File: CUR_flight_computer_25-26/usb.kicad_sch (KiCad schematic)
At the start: 4 parts, among them J1 USB_C_Receptacle_USB2.0_16P, U3 USBLC6-2SC6

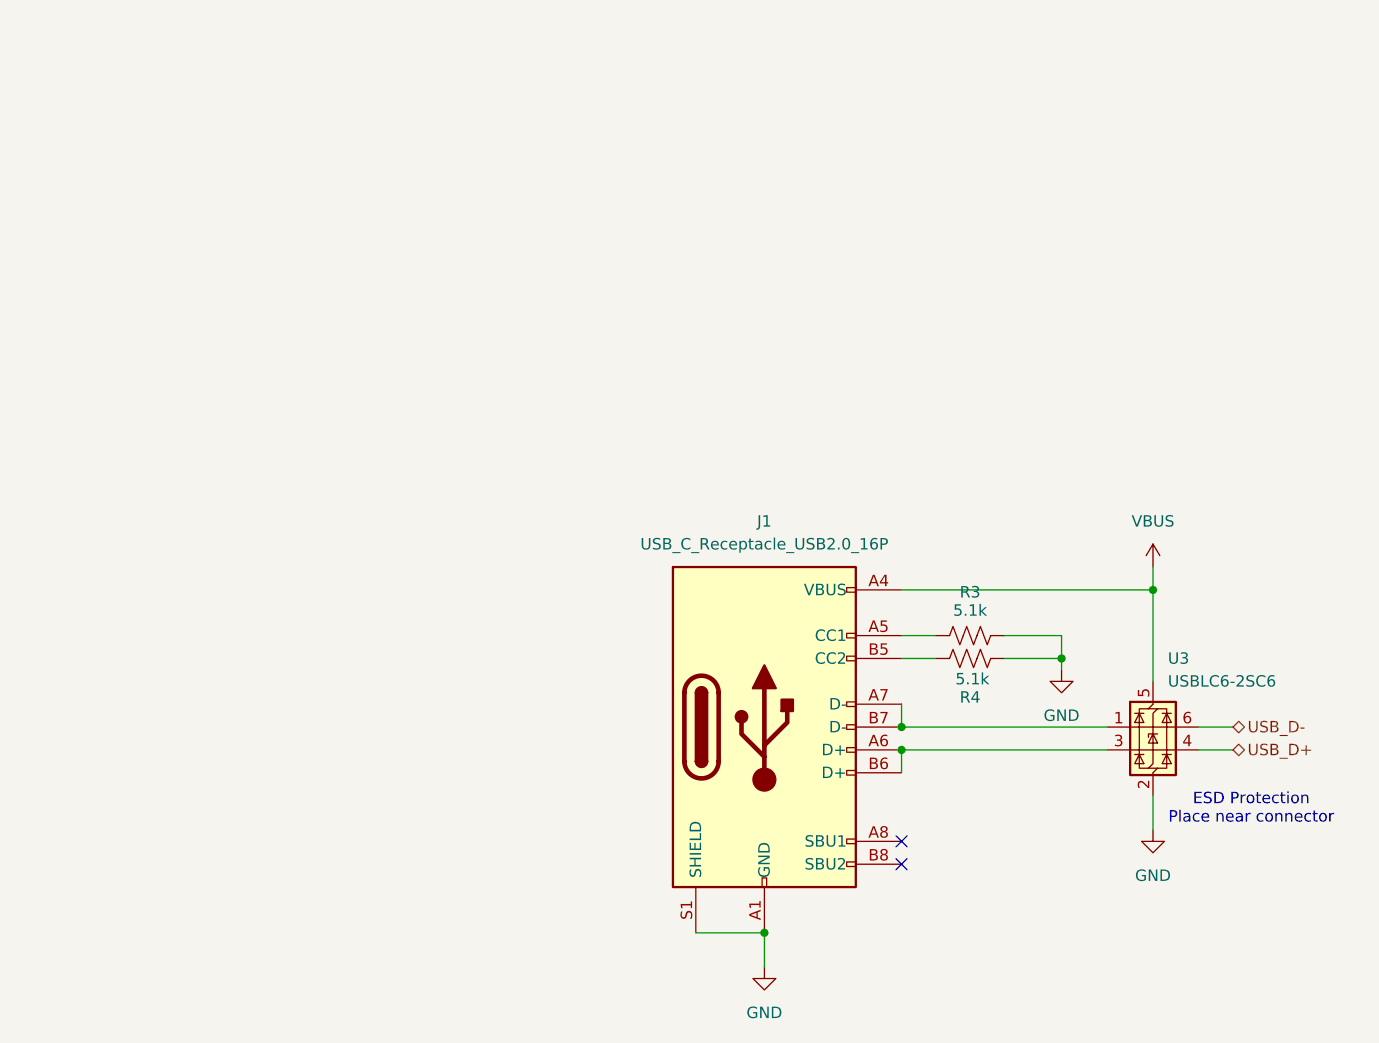
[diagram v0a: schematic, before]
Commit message: MCU work
added decoupling, reset button

need to figure out vddusb
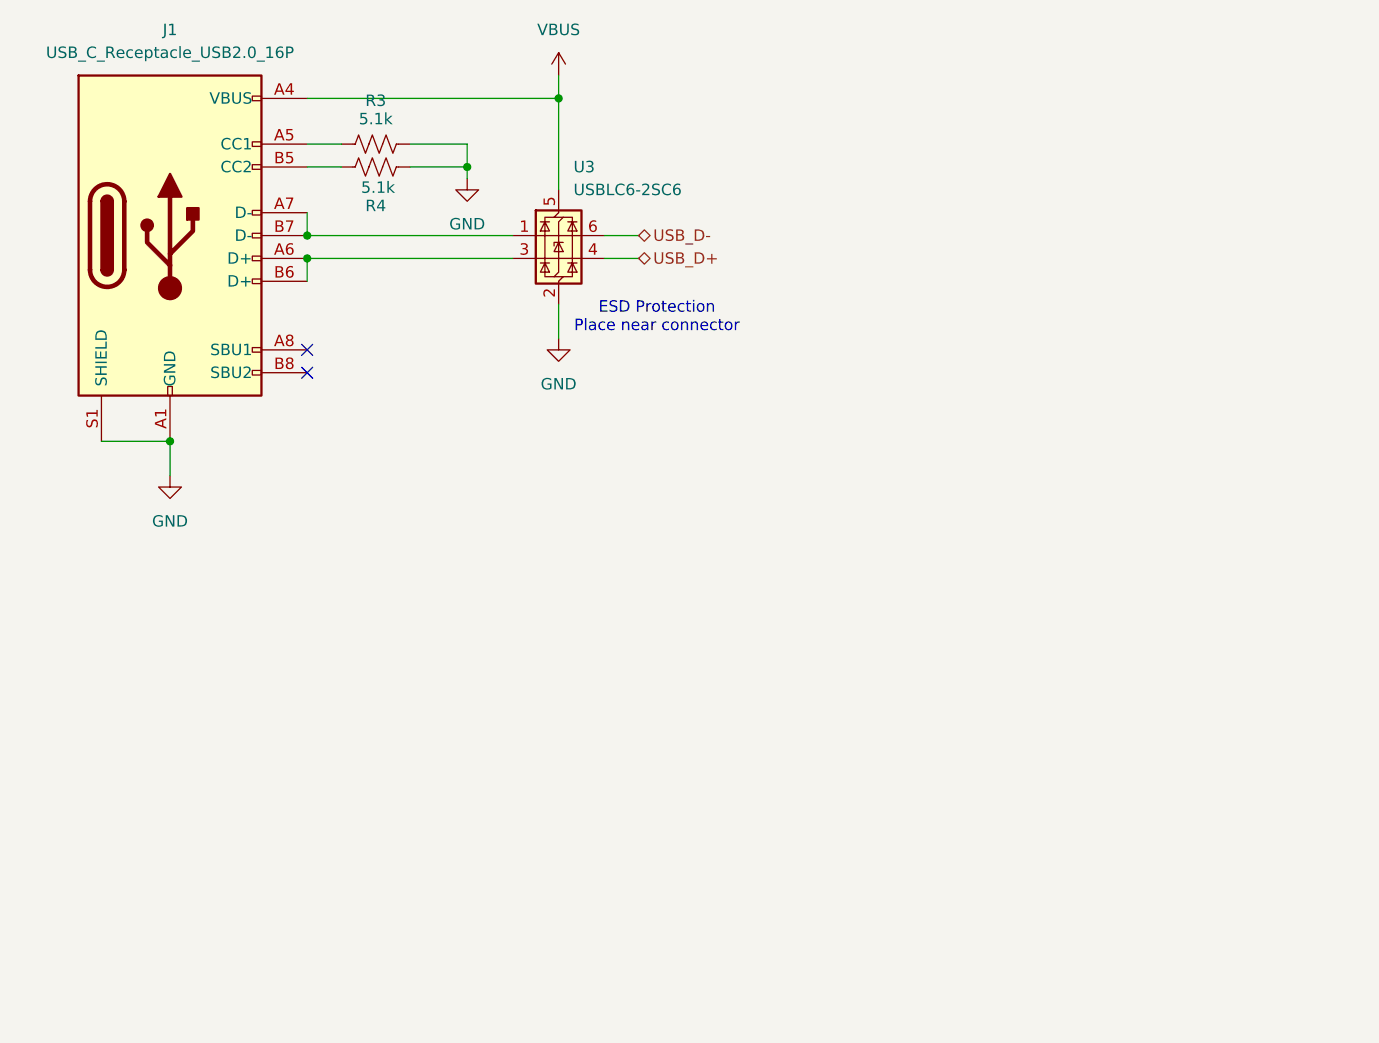
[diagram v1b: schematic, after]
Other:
- moved on the sheet: J1, R3, R4, U3

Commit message: Implement RF reference design for LoRA module
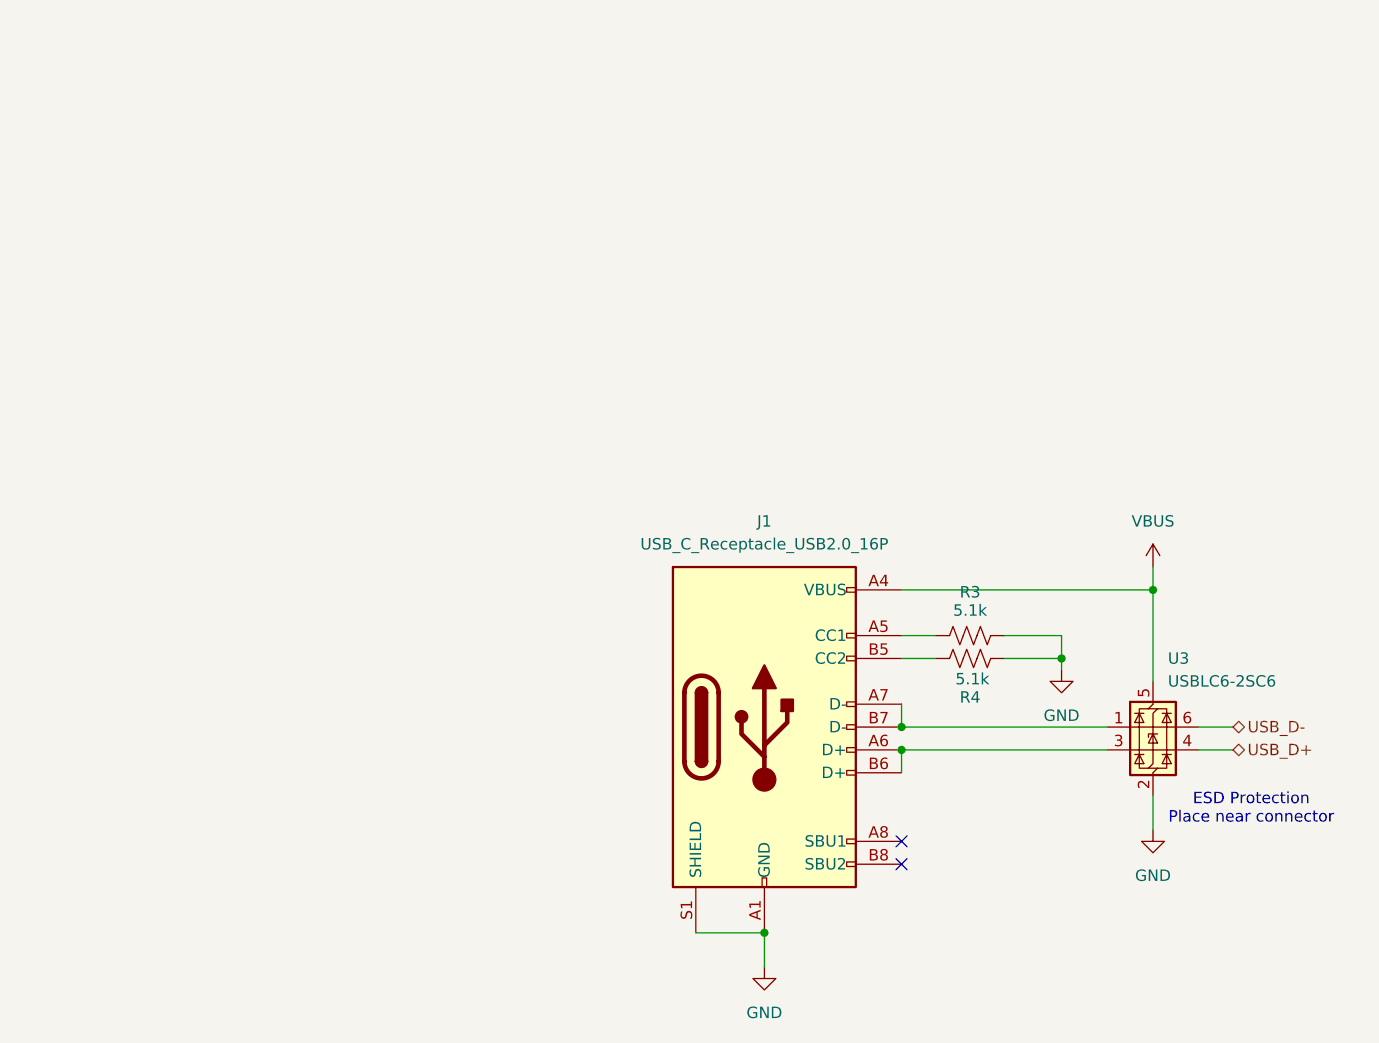
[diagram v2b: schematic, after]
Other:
- moved on the sheet: J1, R3, R4, U3
